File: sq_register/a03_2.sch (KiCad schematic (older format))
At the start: 26 parts, among them U3026 74HC02, U3027 74HC04, U3028 74HC02, U3029 74HC27, U3030 74HC02, U3031 74HC02, U3032 74HC27, U3033 74LVC07, U3034 74HC04, U3035 74HC02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

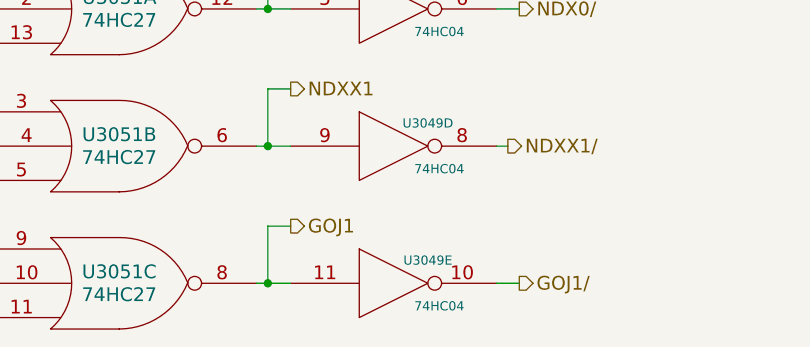
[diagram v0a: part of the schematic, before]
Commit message: Added the 'stage' bit of the Stage Branch Decoder module, and cleaned up a lot of initial conditions (still probably a lot to be done there)
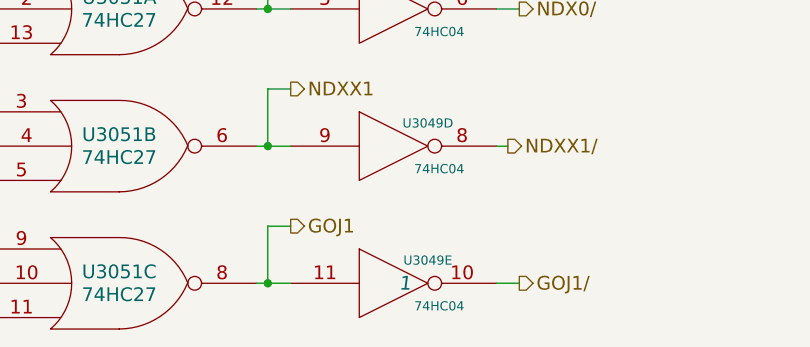
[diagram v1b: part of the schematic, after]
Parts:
- U3049: Initial (none) -> 1
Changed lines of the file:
@@
 F 2 "" H 16400 12950 60  0000 C CNN
 F 3 "" H 16400 12950 60  0000 C CNN
+F 4 "1" H 16450 12950 60  0000 C CIN "Initial"
 	5    16400 12950
 	1    0    0    -1

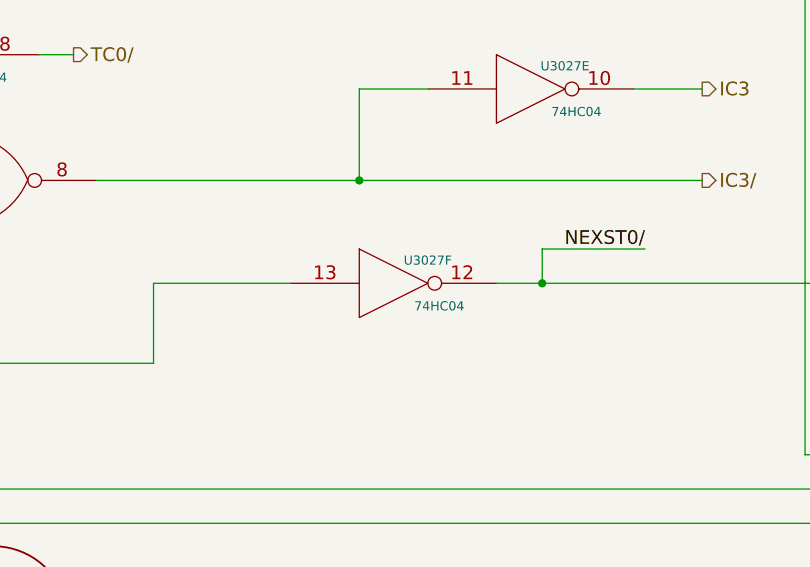
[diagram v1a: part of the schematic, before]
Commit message: More initial conditions fixes, prevents STG3 from oscillating and freqking out TC0
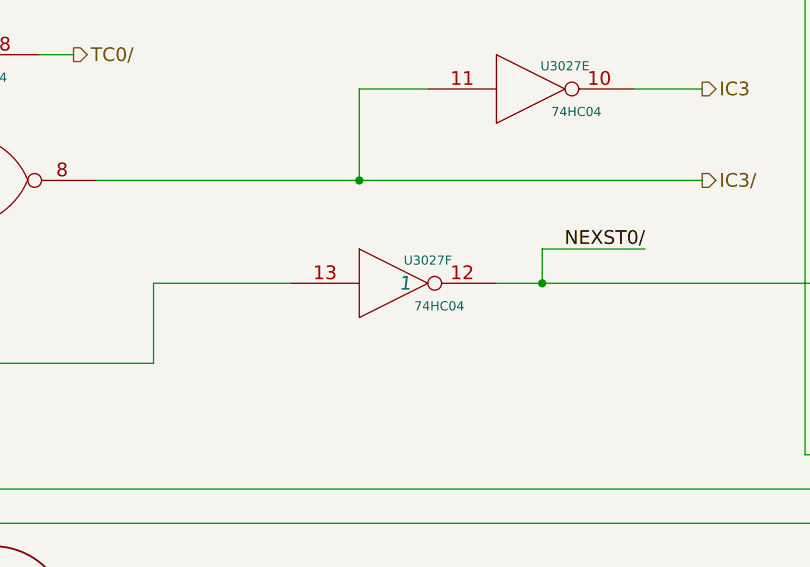
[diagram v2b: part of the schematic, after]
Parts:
- U3027: Initial (none) -> 1
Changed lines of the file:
@@
 F 2 "" H 5600 5700 60  0000 C CNN
 F 3 "" H 5600 5700 60  0000 C CNN
+F 4 "1" H 5650 5700 60  0000 C CIN "Initial"
 	6    5600 5700
 	1    0    0    -1

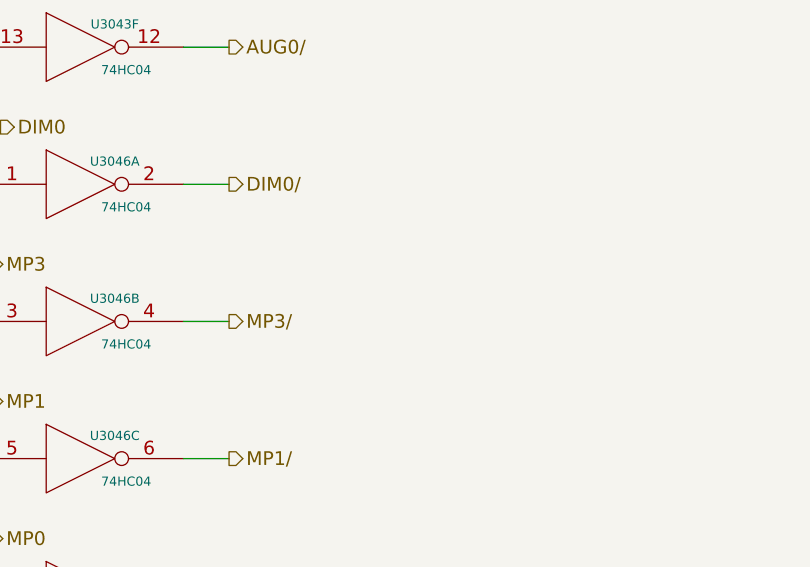
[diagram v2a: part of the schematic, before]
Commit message: Added page 2 of the Stage Branch Decoding module, and tied it into the rest of the system
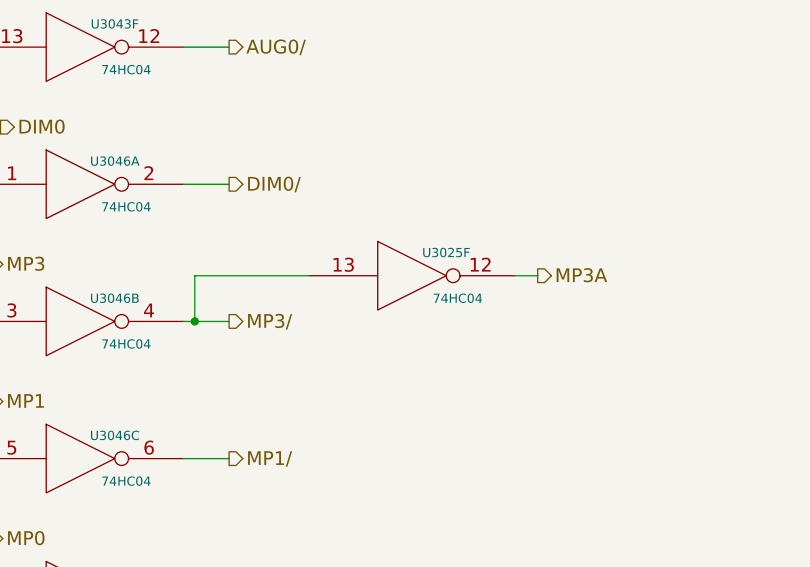
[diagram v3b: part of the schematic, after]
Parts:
- added U3025: 74HC04, symbol 74HC04
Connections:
- net GND: now also U3025.7 (GND)
- net MP3/: now also U3025.13
- net VCC: now also U3025.14 (VCC)
- new net MP3A: U3025.12
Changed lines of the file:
@@
 	1250 7250 1250 3950
 Connection ~ 1250 3950
+$Comp
+L 74HC04 U3025
+U 6 1 5654F4BD
+P 17850 6750
+F 0 "U3025" H 18000 6850 40  0000 C CNN
+F 1 "74HC04" H 18050 6650 40  0000 C CNN
+F 2 "" H 17850 6750 60  0000 C CNN
+F 3 "" H 17850 6750 60  0000 C CNN
+	6    17850 6750
+	1    0    0    -1
+$EndComp
+Wire Wire Line
+	17400 6750 16900 6750
+Wire Wire Line
+	16900 6750 16900 6950
+Connection ~ 16900 6950
+Wire Wire Line
+	18300 6750 18400 6750
+Text HLabel 18400 6750 2    60   Output ~ 0
+MP3A
 $EndSCHEMATC

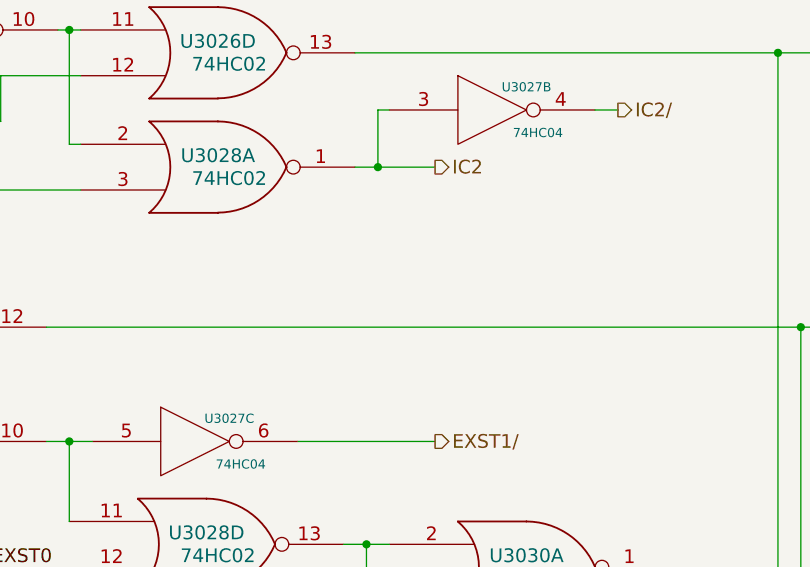
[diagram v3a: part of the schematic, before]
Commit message: Finished the second page of crosspoint generator 1 and tied it into the rest of the system.
Turns out most documentation online is wrong, and block 2 modules have 276 pins per module to the backplane, rather than the 140-144 that is quoted everywhere (those are block 1 figures). Instead of dealing with connector selection again, I opted to just add another row to the '128-pin' connector. I'll fix that more properly later
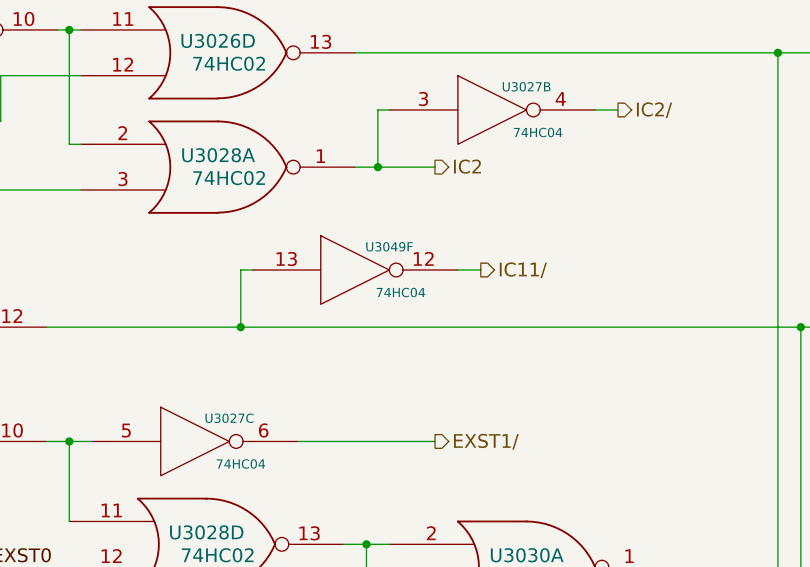
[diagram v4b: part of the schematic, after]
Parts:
- added unit 6 of U3049
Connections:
- net GND: now also U3049.7 (GND)
- net IC11: now also U3049.13
- net VCC: now also U3049.14 (VCC)
- new net IC11/: U3049.12
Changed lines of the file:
@@
 Text HLabel 18400 6750 2    60   Output ~ 0
 MP3A
+$Comp
+L 74HC04 U3049
+U 6 1 567E74A4
+P 5550 2450
+F 0 "U3049" H 5700 2550 40  0000 C CNN
+F 1 "74HC04" H 5750 2350 40  0000 C CNN
+F 2 "" H 5550 2450 60  0000 C CNN
+F 3 "" H 5550 2450 60  0000 C CNN
+	6    5550 2450
+	1    0    0    -1
+$EndComp
+Text HLabel 6100 2450 2    60   Output ~ 0
+IC11/
+Wire Wire Line
+	5100 2450 5050 2450
+Wire Wire Line
+	5050 2450 5050 2700
+Wire Wire Line
+	6000 2450 6100 2450
+Connection ~ 5050 2700
 $EndSCHEMATC

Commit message: Tied in module 7, and corrected lots of errors.
Off the top of my head:
* T12DC/ not actually connected to restart logic in A02-2
* IC12/ and IC13 schematic errors
* Lots of gates moved from later modules up to modules 2-7
* YT0..7 logic dropped from 7, it belongs in 14
* Lots of missing signal breakouts
* ...probably some other things, I should keep a list as I go

All control pulses associated with GOJ1 now behave correctly during
GOJ1.
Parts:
- added R3002: R, symbol R
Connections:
- net CCS0: now also U3042.8
- net CCS0/: no longer U3042.8
- net IC13/: now also R3002.2
- net VCC: now also R3002.1
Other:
- moved on the sheet: U3027F
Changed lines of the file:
@@
 L 74HC04 U3027
 U 6 1 56310285
-P 5600 5700
-F 0 "U3027" H 5750 5800 40  0000 C CNN
-F 1 "74HC04" H 5800 5600 40  0000 C CNN
-F 2 "" H 5600 5700 60  0000 C CNN
-F 3 "" H 5600 5700 60  0000 C CNN
-F 4 "1" H 5650 5700 60  0000 C CIN "Initial"
-	6    5600 5700
+P 5600 5550
+F 0 "U3027" H 5750 5650 40  0000 C CNN
+F 1 "74HC04" H 5800 5450 40  0000 C CNN
+F 2 "" H 5600 5550 60  0000 C CNN
+F 3 "" H 5600 5550 60  0000 C CNN
+F 4 "1" H 5650 5550 60  0000 C CIN "Initial"
+	6    5600 5550
 	1    0    0    -1
 $EndComp
@@
 Text Label 3500 5900 2    60   ~ 0
 NEXST0
-Text Label 6700 5550 2    60   ~ 0
+Text Label 6500 5550 2    60   ~ 0
 NEXST0/
 $Comp
@@
 Connection ~ 1150 5400
 Wire Wire Line
-	4550 6050 4550 5700
-Wire Wire Line
-	4550 5700 5150 5700
+	4550 6050 4550 5550
+Wire Wire Line
+	4550 5550 5150 5550
 Connection ~ 3050 6050
 Wire Wire Line
-	6050 5700 10550 5700
+	6050 5550 10550 5550
 Wire Wire Line
 	2900 7150 3250 7150
@@
 	8950 6600 9050 6600
 Wire Wire Line
-	9950 6150 9950 6600
+	9950 6100 9950 6600
 Wire Wire Line
 	7700 4250 7700 6000
@@
 	1250 7800 1250 12050
 Connection ~ 1250 7800
-Wire Wire Line
-	6250 5700 6250 5550
-Wire Wire Line
-	6250 5550 6700 5550
-Connection ~ 6250 5700
 Wire Wire Line
 	1150 9100 1700 9100
@@
 Connection ~ 14400 1600
 Wire Wire Line
-	10550 5700 10550 2900
+	10550 5550 10550 2900
 Wire Wire Line
 	10550 2900 14600 2900
@@
 	15800 2750 16050 2750
 Wire Wire Line
-	15950 2750 15950 2550
+	15950 2550 15950 2950
 Wire Wire Line
 	15950 2550 16000 2550
@@
 $EndComp
 Wire Wire Line
-	17350 2750 17350 2900
-Wire Wire Line
-	17350 2900 19100 2900
-Wire Wire Line
-	19100 2900 19100 3300
-Wire Wire Line
 	19100 3300 19350 3300
-Connection ~ 17350 2750
 Wire Wire Line
 	19350 3500 19100 3500
@@
 	6000 2450 6100 2450
 Connection ~ 5050 2700
+$Comp
+L R R3002
+U 1 1 56B1DF19
+P 9950 5950
+F 0 "R3002" V 10030 5950 50  0000 C CNN
+F 1 "R" V 9950 5950 50  0000 C CNN
+F 2 "" V 9880 5950 30  0000 C CNN
+F 3 "" H 9950 5950 30  0000 C CNN
+	1    9950 5950
+	1    0    0    -1
+$EndComp
+Connection ~ 9950 6150
+$Comp
+L VCC #PWR07
+U 1 1 56B1E5D8
+P 9950 5800
+F 0 "#PWR07" H 9950 5650 50  0001 C CNN
+F 1 "VCC" H 9950 5950 50  0000 C CNN
+F 2 "" H 9950 5800 60  0000 C CNN
+F 3 "" H 9950 5800 60  0000 C CNN
+	1    9950 5800
+	1    0    0    -1
+$EndComp
+Wire Wire Line
+	15950 2950 19100 2950
+Wire Wire Line
+	19100 2950 19100 3300
 $EndSCHEMATC

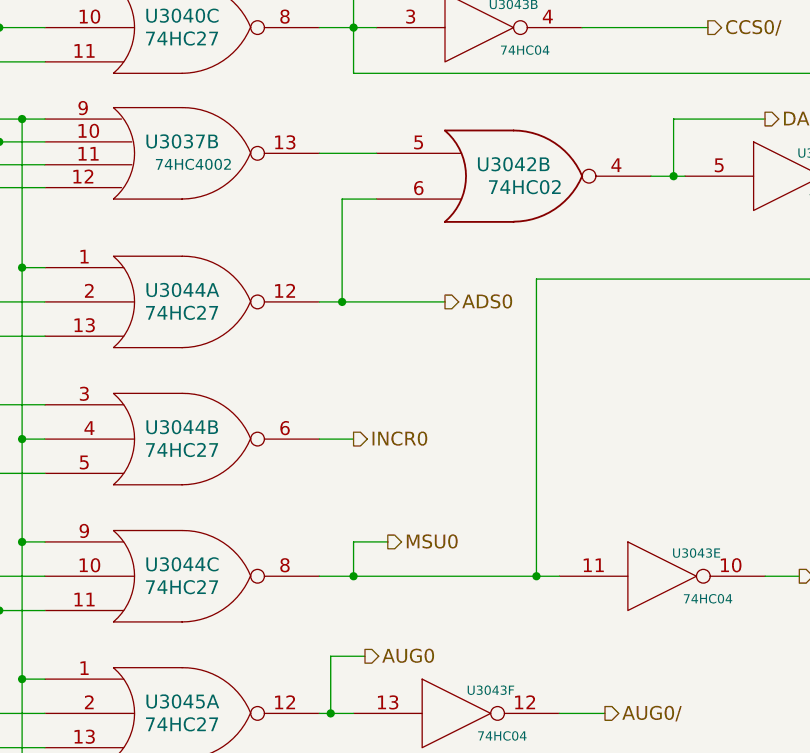
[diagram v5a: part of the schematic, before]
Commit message: Tied in module 8, and corrected lots of initial conditions.
The registers and ALU appear to work now, with TC0 and STD2 shuffling things around correctly, and Z counting up as instructions execute.
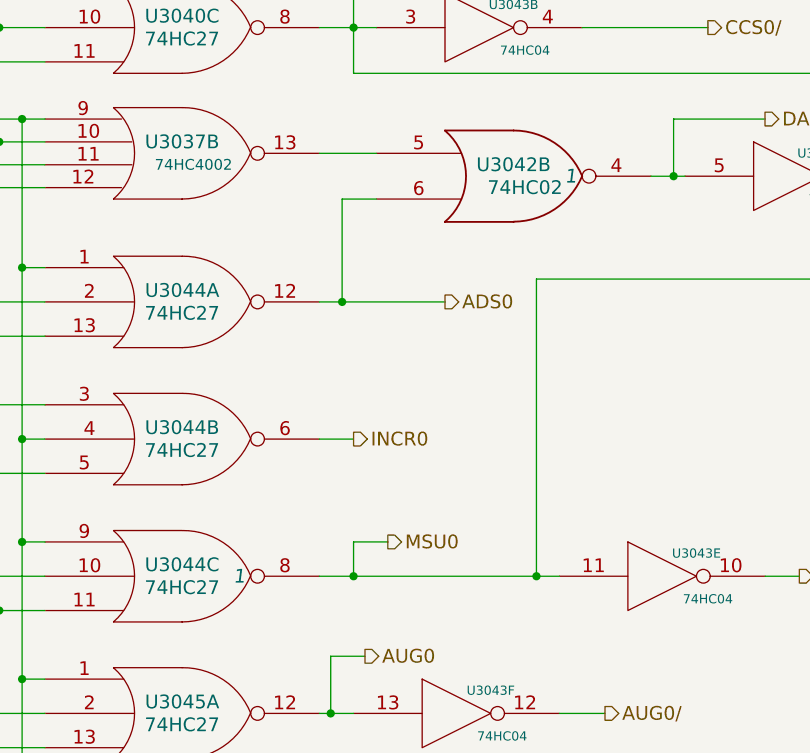
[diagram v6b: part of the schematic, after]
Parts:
- U3042, U3044: Initial (none) -> 1
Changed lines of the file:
@@
 F 2 "" H 16650 3400 60  0000 C CNN
 F 3 "" H 16650 3400 60  0000 C CNN
+F 4 "1" H 16900 3400 60  0000 C CIN "Initial"
 	2    16650 3400
 	1    0    0    -1
@@
 F 2 "" H 15200 5150 60  0000 C CNN
 F 3 "" H 15200 5150 60  0000 C CNN
+F 4 "1" H 15450 5150 60  0000 C CIN "Initial"
 	3    15200 5150
 	1    0    0    -1

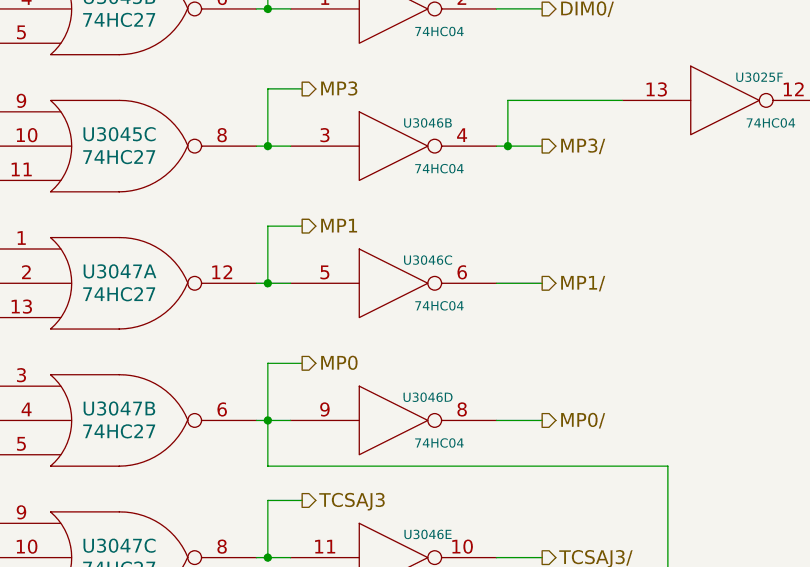
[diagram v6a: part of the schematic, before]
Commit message: Added the final four bit module. All 16 bits of the central/special registers are present. We're stuck at address 0 because TC is using RAD, which needs to be translated into RG or RZ by module 12
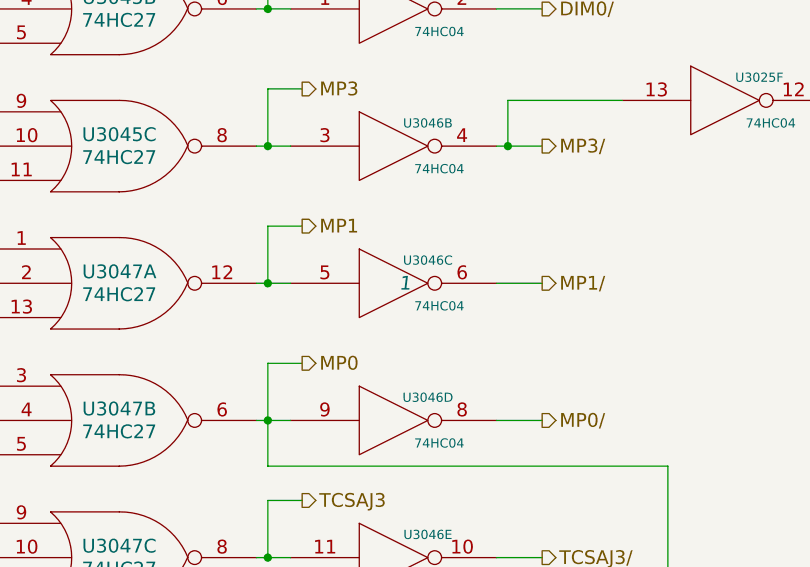
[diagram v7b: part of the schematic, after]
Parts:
- U3046: Initial (none) -> 1
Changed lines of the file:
@@
 F 2 "" H 16400 7550 60  0000 C CNN
 F 3 "" H 16400 7550 60  0000 C CNN
+F 4 "1" H 16450 7550 60  0000 C CIN "Initial"
 	3    16400 7550
 	1    0    0    -1

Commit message: Updated fixed memory model, plus various bugfixes
Rope memory control signals are now decoded much earlier in the cycle to
determine the target address, allowing slower memory devices (such as
the EPCS on the DE0 Nano) enough time to load their data.

The bugfixes are mostly wiring errors discovered by debugging lockups in
when running Colossus 237 -- all were causing the ST2 pulse to not
occur, so errors that *don't* prevent ST2 from happening very well might
be present in the instructions that have been fixed.

The computer now gets through the initialization code and enters an
infinite loop when attempting to invoke the interpeter, due to the lack
of erasable memory.
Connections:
- net QC0: now also U3040.2, U3040.4
- net QC0/: no longer U3040.2, U3040.4
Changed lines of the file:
@@
 SQ1/
 Text HLabel 13550 1100 0    60   Input ~ 0
-QC0/
+QC0
 Text Label 13250 1250 0    60   ~ 0
 EXST0/
@@
 	16900 1100 17250 1100
 Wire Wire Line
-	14400 1100 14400 11900
-Wire Wire Line
 	14400 1600 14600 1600
 Connection ~ 14400 1100
@@
 Connection ~ 14300 950
 Wire Wire Line
-	14400 2750 14600 2750
-Connection ~ 14400 1600
+	13200 2750 14600 2750
 Wire Wire Line
 	10550 5550 10550 2900
@@
 Wire Wire Line
 	19100 2950 19100 3300
+Wire Wire Line
+	14400 1100 14400 1600
+Text HLabel 13200 2750 0    60   Input ~ 0
+QC0/
+Wire Wire Line
+	14400 2750 14400 11900
 $EndSCHEMATC
